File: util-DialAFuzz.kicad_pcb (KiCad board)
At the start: 2 copper layers, 9.5 x 21.2 mm, 5 parts, among them J1 Conn_01x03_Pin, Q1 BC847, Q2 BC847

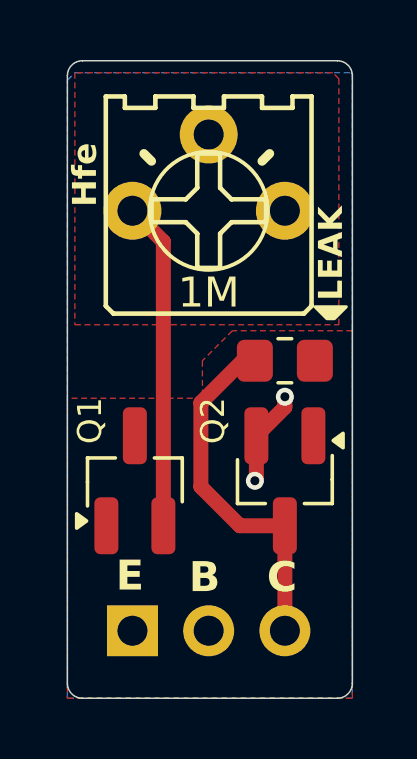
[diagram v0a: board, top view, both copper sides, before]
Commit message: v0.2: compact double-sided layout, trimmer on the back (9.5 x 15.8 mm)
Same Widlar circuit as v0.1; the through-hole trimmer moves to the back
side so the SMD parts and header fit a 5.4 mm shorter board.

Co-Authored-By: Claude Fable 5.1 <noreply@anthropic.com>
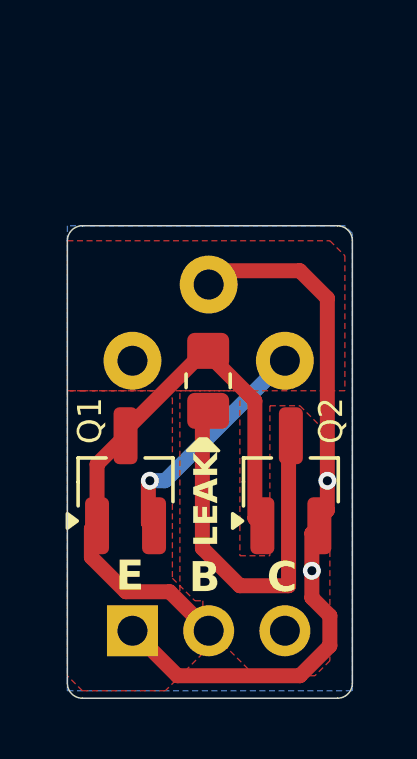
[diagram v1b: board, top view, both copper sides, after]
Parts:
- RV1: moved to B.Cu
- moved RV1 5.00 mm to (100.5, 79.0), turned to 180 degrees
- moved R2 2.64 mm to (100.4, 79.7), turned to 90 degrees
- moved Q1 0.31 mm to (97.7, 83.0)
- moved Q2 0.20 mm to (103.2, 83.0), turned to 90 degrees
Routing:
- net EMITTER: track 3.21 -> 24.2 mm
- net BASE: track 0.00 -> 20.2 mm
- net Net-(Q1-E): track 10.9 -> 7.81 mm, vias 0 -> 1
- net COLLECTOR: track 12.0 -> 13.1 mm
- added copper zone on F.Cu, net COLLECTOR
- added copper zone on F.Cu, net EMITTER
- removed copper zone on F.Cu, net Net-(Q1-E)
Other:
- board size 9.5 x 21.2 mm -> 9.5 x 15.8 mm
- board text added: "z2a Dial -a- Fuzz"
- board text removed: "z2a Dial-a-Fuzz"
